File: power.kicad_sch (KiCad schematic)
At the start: 16 parts, among them Q1 IRLML6402, SW1 SW_SPDT, U1 AZ1117-5.0, U2 AZ1117-3.3

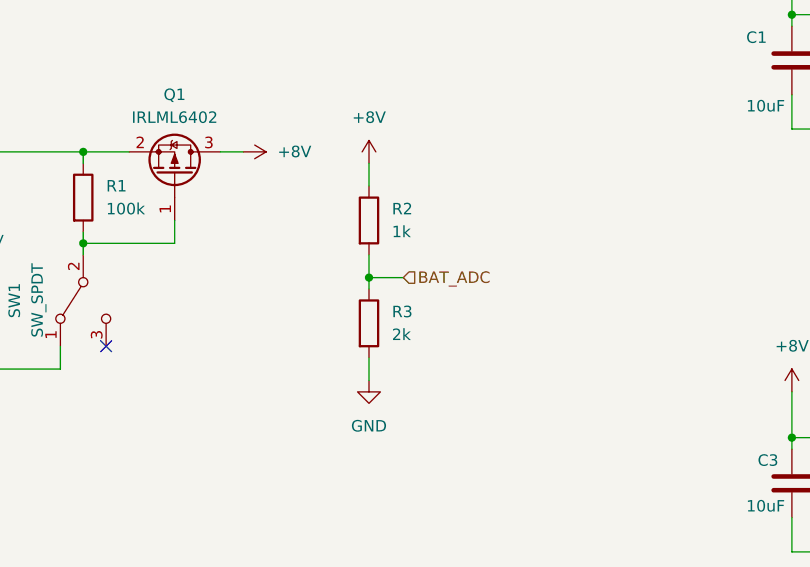
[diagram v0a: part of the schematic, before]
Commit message: 分圧の抵抗値が間違っていたので修正
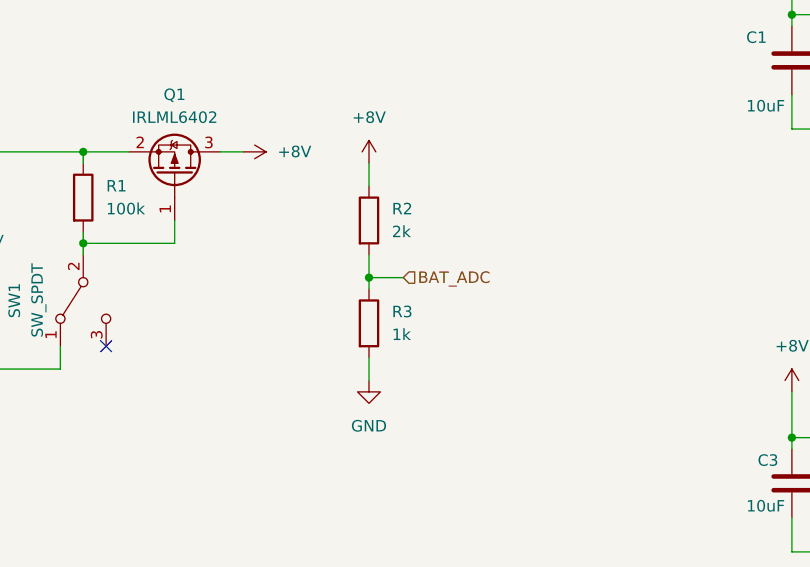
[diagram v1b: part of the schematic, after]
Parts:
- R2: value 1k -> 2k
- R3: value 2k -> 1k
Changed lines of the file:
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@@
       (effects (font (size 1.27 1.27)) (justify left))
     )
-    (property "Value" "1k" (at 124.46 97.79 0)
+    (property "Value" "2k" (at 124.46 97.79 0)
       (effects (font (size 1.27 1.27)) (justify left))
     )
@@
       (effects (font (size 1.27 1.27)) (justify left))
     )
-    (property "Value" "2k" (at 124.46 109.22 0)
-      (effects (font (size 1.27 1.27)) (justify left))
-    )
+    (property "Value" "1k" (at 124.46 109.22 0)
+      (effects (font (size 1.27 1.27)) (justify left))
+    )

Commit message: アノテーション番号ミスの修正とフットプリント割り当て途中（部品リストも途中生成）
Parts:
- C1, C2, C3, C4: footprint (none) -> Capacitor_SMD:C_0603_1608Metric_Pad1.08x0.95mm_HandSolder
- D1, D2: footprint (none) -> LED_SMD:LED_0603_1608Metric_Pad1.05x0.95mm_HandSolder
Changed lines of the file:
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@@
       (effects (font (size 1.27 1.27)) (justify left))
     )
-    (property "Footprint" "" (at 190.1952 129.54 0)
+    (property "Footprint" "Capacitor_SMD:C_0603_1608Metric_Pad1.08x0.95mm_HandSolder" (at 190.1952 129.54 0)
       (effects (font (size 1.27 1.27)) hide)
     )
@@
       (effects (font (size 1.27 1.27)) (justify left))
     )
-    (property "Footprint" "" (at 169.8752 82.55 0)
+    (property "Footprint" "Capacitor_SMD:C_0603_1608Metric_Pad1.08x0.95mm_HandSolder" (at 169.8752 82.55 0)
       (effects (font (size 1.27 1.27)) hide)
     )
@@
       (effects (font (size 1.27 1.27)) (justify right))
     )
-    (property "Footprint" "" (at 200.66 83.82 0)
+    (property "Footprint" "LED_SMD:LED_0603_1608Metric_Pad1.05x0.95mm_HandSolder" (at 200.66 83.82 0)
       (effects (font (size 1.27 1.27)) hide)
     )
@@
         )
         (path "/588ca8cd-b11b-4b55-96d9-278aac6cd0cf/095bf668-b079-4330-a0e4-b1270338e20d"
-          (reference "D1") (unit 1)
+          (reference "D2_1") (unit 1)
         )
       )
@@
       (effects (font (size 1.27 1.27)) (justify right))
     )
-    (property "Footprint" "" (at 200.66 130.81 0)
+    (property "Footprint" "LED_SMD:LED_0603_1608Metric_Pad1.05x0.95mm_HandSolder" (at 200.66 130.81 0)
       (effects (font (size 1.27 1.27)) hide)
     )
@@
         )
         (path "/588ca8cd-b11b-4b55-96d9-278aac6cd0cf/095bf668-b079-4330-a0e4-b1270338e20d"
-          (reference "D2") (unit 1)
+          (reference "D2_2") (unit 1)
         )
       )
@@
       (effects (font (size 1.27 1.27)) (justify left))
     )
-    (property "Footprint" "" (at 190.1952 82.55 0)
+    (property "Footprint" "Capacitor_SMD:C_0603_1608Metric_Pad1.08x0.95mm_HandSolder" (at 190.1952 82.55 0)
       (effects (font (size 1.27 1.27)) hide)
     )
@@
       (effects (font (size 1.27 1.27)) (justify left))
     )
-    (property "Footprint" "" (at 169.8752 129.54 0)
-      (effects (font (size 1.27 1.27)) hide)
-    )
+    (property "Footprint" "Capacitor_SMD:C_0603_1608Metric_Pad1.08x0.95mm_HandSolder" (at 169.8752 129.54 0)
+      (effects (font (size 1.27 1.27)) hide)
+    )

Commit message: フェライトビーズに型番追加し、自作パッケージの構成へこう
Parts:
- R1, R2, R3, R5, R6: footprint (none) -> Resistor_SMD:R_0603_1608Metric_Pad0.98x0.95mm_HandSolder
- U1, U2: footprint (none) -> Package_TO_SOT_SMD:SOT-223
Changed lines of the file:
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@@
       (effects (font (size 1.27 1.27)))
     )
-    (property "Footprint" "" (at 179.07 67.31 0)
+    (property "Footprint" "Package_TO_SOT_SMD:SOT-223" (at 179.07 67.31 0)
       (effects (font (size 1.27 1.27) italic) hide)
     )
@@
       (effects (font (size 1.27 1.27)) (justify left))
     )
-    (property "Footprint" "" (at 120.142 96.52 90)
+    (property "Footprint" "Resistor_SMD:R_0603_1608Metric_Pad0.98x0.95mm_HandSolder" (at 120.142 96.52 90)
       (effects (font (size 1.27 1.27)) hide)
     )
@@
       (effects (font (size 1.27 1.27)) (justify left))
     )
-    (property "Footprint" "" (at 120.142 107.95 90)
+    (property "Footprint" "Resistor_SMD:R_0603_1608Metric_Pad0.98x0.95mm_HandSolder" (at 120.142 107.95 90)
       (effects (font (size 1.27 1.27)) hide)
     )
@@
       (effects (font (size 1.27 1.27)) (justify left))
     )
-    (property "Footprint" "" (at 198.882 77.47 90)
+    (property "Footprint" "Resistor_SMD:R_0603_1608Metric_Pad0.98x0.95mm_HandSolder" (at 198.882 77.47 90)
       (effects (font (size 1.27 1.27)) hide)
     )
@@
       (effects (font (size 1.27 1.27)))
     )
-    (property "Footprint" "" (at 179.07 114.3 0)
+    (property "Footprint" "Package_TO_SOT_SMD:SOT-223" (at 179.07 114.3 0)
       (effects (font (size 1.27 1.27) italic) hide)
     )
@@
       (effects (font (size 1.27 1.27)) (justify left))
     )
-    (property "Footprint" "" (at 88.392 93.98 90)
+    (property "Footprint" "Resistor_SMD:R_0603_1608Metric_Pad0.98x0.95mm_HandSolder" (at 88.392 93.98 90)
       (effects (font (size 1.27 1.27)) hide)
     )
@@
       (effects (font (size 1.27 1.27)) (justify left))
     )
-    (property "Footprint" "" (at 198.882 124.46 90)
-      (effects (font (size 1.27 1.27)) hide)
-    )
+    (property "Footprint" "Resistor_SMD:R_0603_1608Metric_Pad0.98x0.95mm_HandSolder" (at 198.882 124.46 90)
+      (effects (font (size 1.27 1.27)) hide)
+    )

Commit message: スイッチ以外のフットプリント割当完了
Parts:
- BT1: footprint (none) -> Connector_JST:JST_PH_B2B-PH-K_1x02_P2.00mm_Vertical
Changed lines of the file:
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@@
       (effects (font (size 1.27 1.27)) (justify left))
     )
-    (property "Footprint" "" (at 71.12 96.266 90)
+    (property "Footprint" "Connector_JST:JST_PH_B2B-PH-K_1x02_P2.00mm_Vertical" (at 71.12 96.266 90)
       (effects (font (size 1.27 1.27)) hide)
     )

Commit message: 秋月電子のスライドスイッチのフットプリントを追加して全てのフットプリント割当も完了
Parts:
- SW1: footprint (none) -> Self-Made_Generic_Packages:SW_Slide_SS12D01G4_AKIZUKI
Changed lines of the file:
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@@
       (effects (font (size 1.27 1.27)))
     )
-    (property "Footprint" "" (at 90.17 105.41 0)
+    (property "Footprint" "Self-Made_Generic_Packages:SW_Slide_SS12D01G4_AKIZUKI" (at 90.17 105.41 0)
       (effects (font (size 1.27 1.27)) hide)
     )

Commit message: バッテリ端子のフットプリントを割り当ててネットリストに出力して取り込み
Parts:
- BT1: footprint Connector_JST:JST_PH_B2B-PH-K_1x02_P2.00mm_Vertical -> Self-Made_Generic_Packages:2sBattery
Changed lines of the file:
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@@
       (effects (font (size 1.27 1.27)) (justify left))
     )
-    (property "Footprint" "Connector_JST:JST_PH_B2B-PH-K_1x02_P2.00mm_Vertical" (at 71.12 96.266 90)
+    (property "Footprint" "Self-Made_Generic_Packages:2sBattery" (at 71.12 96.266 90)
       (effects (font (size 1.27 1.27)) hide)
     )

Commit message: レギュレータ２つのフットプリント割り当てを2ピンが２つあるものに変更した
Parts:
- U1, U2: footprint Package_TO_SOT_SMD:SOT-223 -> Package_TO_SOT_SMD:SOT-223-3_TabPin2
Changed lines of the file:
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@@
       (effects (font (size 1.27 1.27)))
     )
-    (property "Footprint" "Package_TO_SOT_SMD:SOT-223" (at 179.07 67.31 0)
+    (property "Footprint" "Package_TO_SOT_SMD:SOT-223-3_TabPin2" (at 179.07 67.31 0)
       (effects (font (size 1.27 1.27) italic) hide)
     )
@@
       (effects (font (size 1.27 1.27)))
     )
-    (property "Footprint" "Package_TO_SOT_SMD:SOT-223" (at 179.07 114.3 0)
+    (property "Footprint" "Package_TO_SOT_SMD:SOT-223-3_TabPin2" (at 179.07 114.3 0)
       (effects (font (size 1.27 1.27) italic) hide)
     )

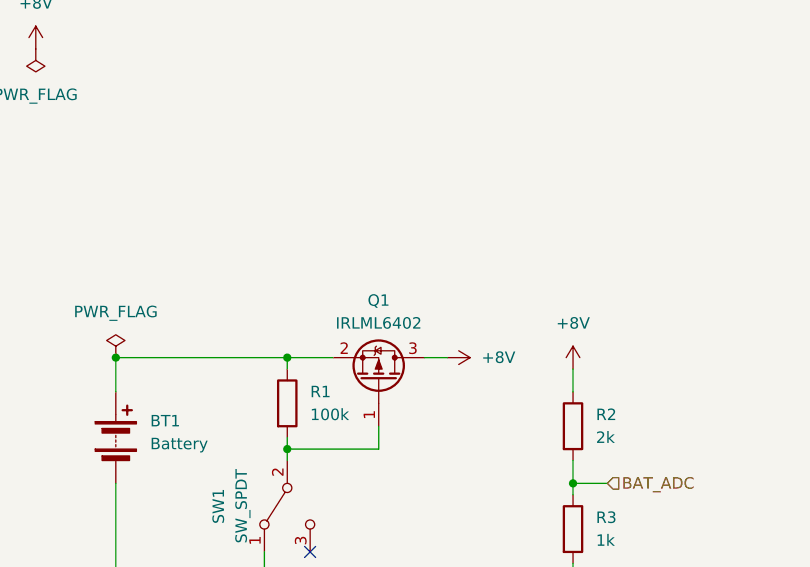
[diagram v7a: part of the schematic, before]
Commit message: AON7421のフットプリント追加
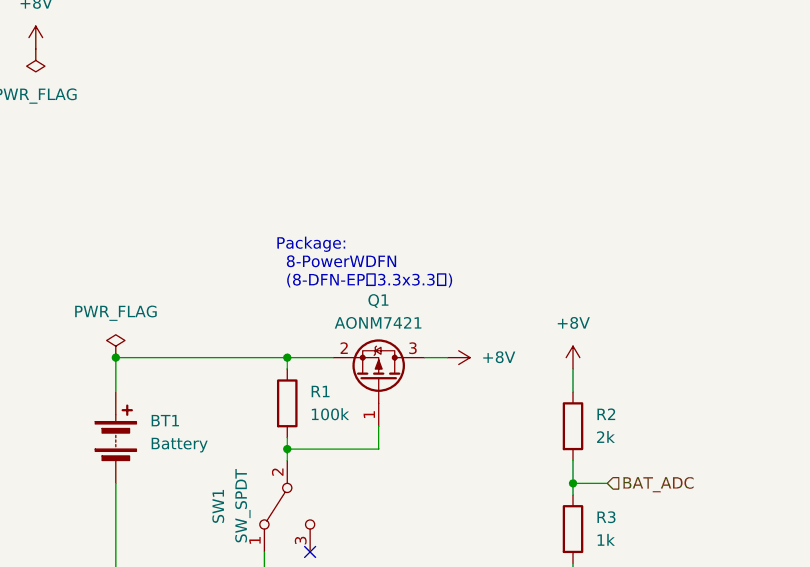
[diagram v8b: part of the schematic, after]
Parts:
- Q1: value IRLML6402 -> AONM7421; footprint Package_TO_SOT_SMD:SOT-23 -> (none)
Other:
- note added: "Package: 8-PowerWDFN (8-DFN-EP（3.3x3.3）)"
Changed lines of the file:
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@@
+    (effects (font (size 1.27 1.27)) (justify left bottom))
+  )
+  (text "Package:\n  8-PowerWDFN \n  (8-DFN-EP（3.3x3.3）)" (at 88.9 81.28 0)
     (effects (font (size 1.27 1.27)) (justify left bottom))
   )
@@
       (effects (font (size 1.27 1.27)))
     )
-    (property "Value" "IRLML6402" (at 100.33 85.09 90)
-      (effects (font (size 1.27 1.27)))
-    )
-    (property "Footprint" "Package_TO_SOT_SMD:SOT-23" (at 98.425 86.36 0)
+    (property "Value" "AONM7421" (at 100.33 85.09 90)
+      (effects (font (size 1.27 1.27)))
+    )
+    (property "Footprint" "" (at 98.425 86.36 0)
       (effects (font (size 1.27 1.27) italic) (justify left) hide)
     )
